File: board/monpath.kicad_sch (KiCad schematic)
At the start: 120 parts, among them J2 BEL_FUSE_0826-1G1T-23-F, J8 BEL_FUSE_0826-1G1T-23-F, U10 ECS-2016MVQ-250-CN-TR, U11 ECS-2016MVQ-250-CN-TR, U12 ECS-2016MVQ-250-CN-TR, U2 KSZ9031RN, U4 XC7S15-1FTGB196C, U9 KSZ9031RN

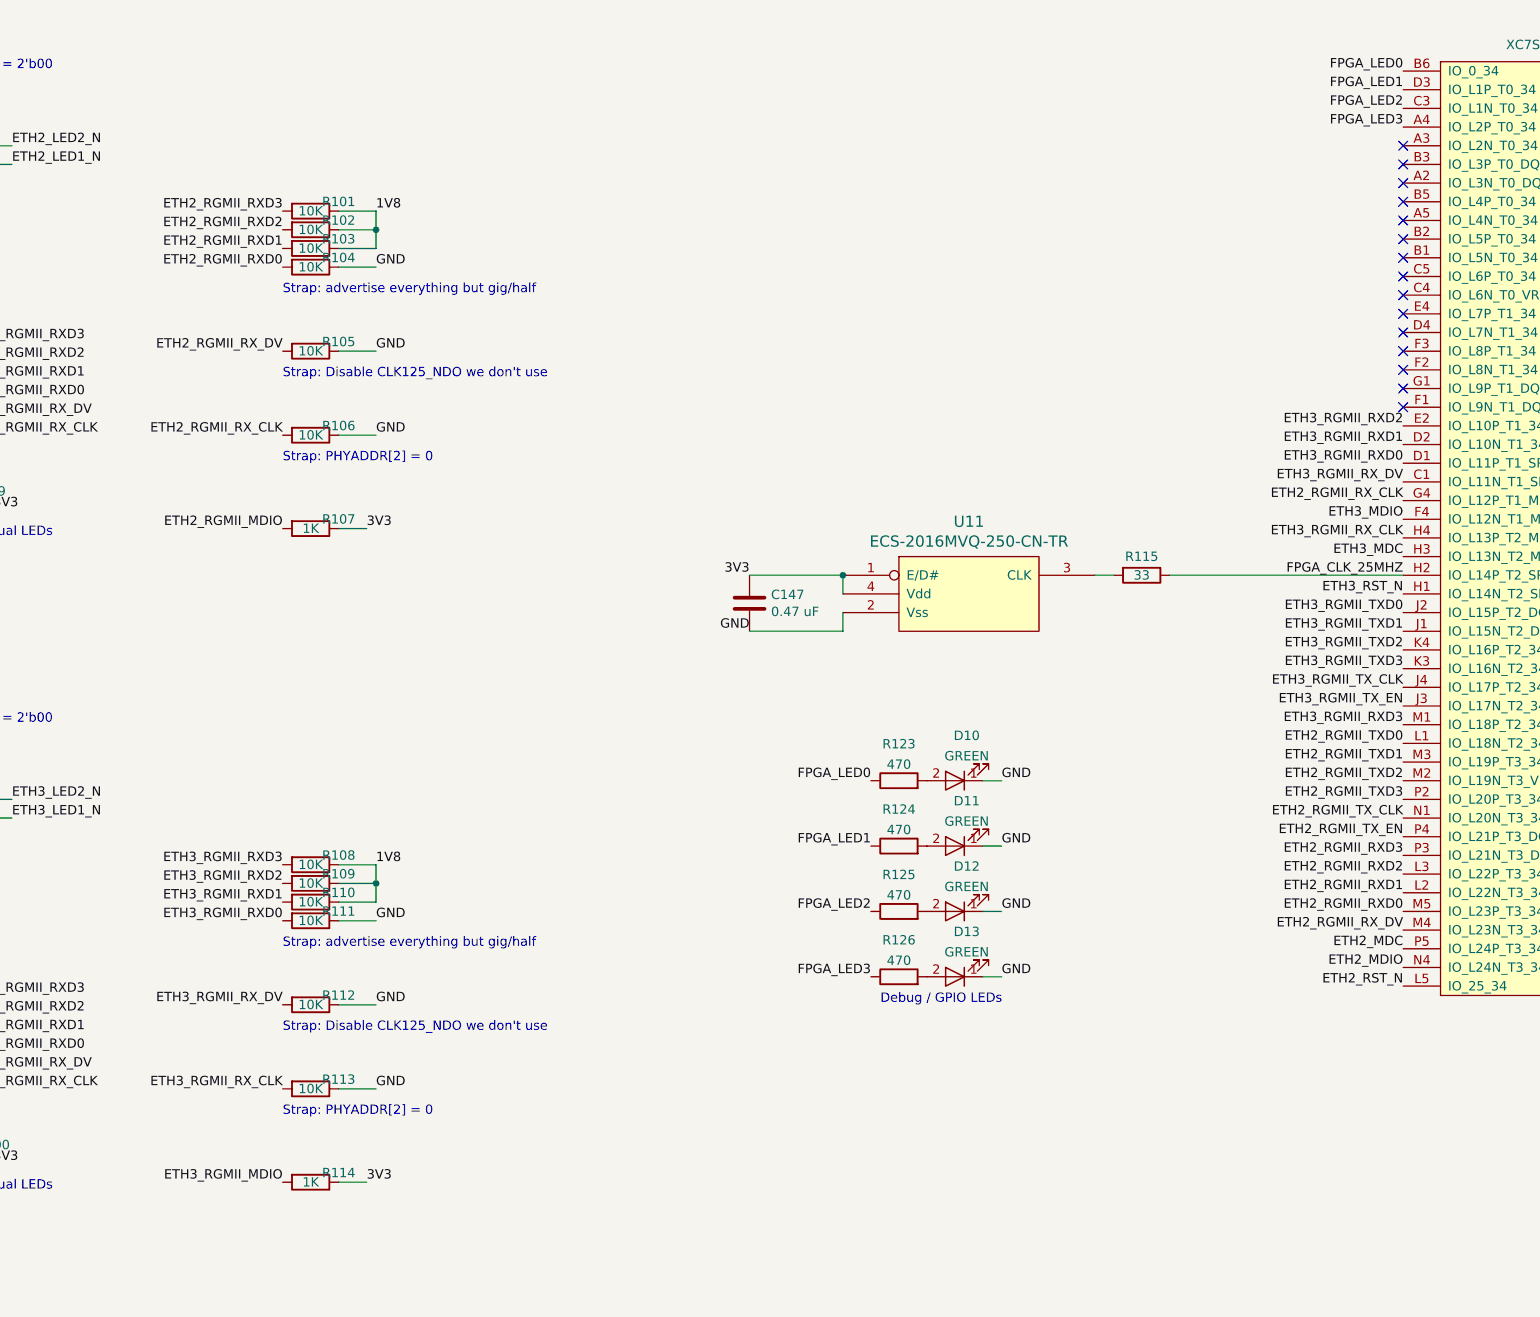
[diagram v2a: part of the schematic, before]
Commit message: Continued initial layout. First PHY fully routed including connection to FPGA. Hooked up 0402 bypass caps under FPGA. Flash is roughly placed.
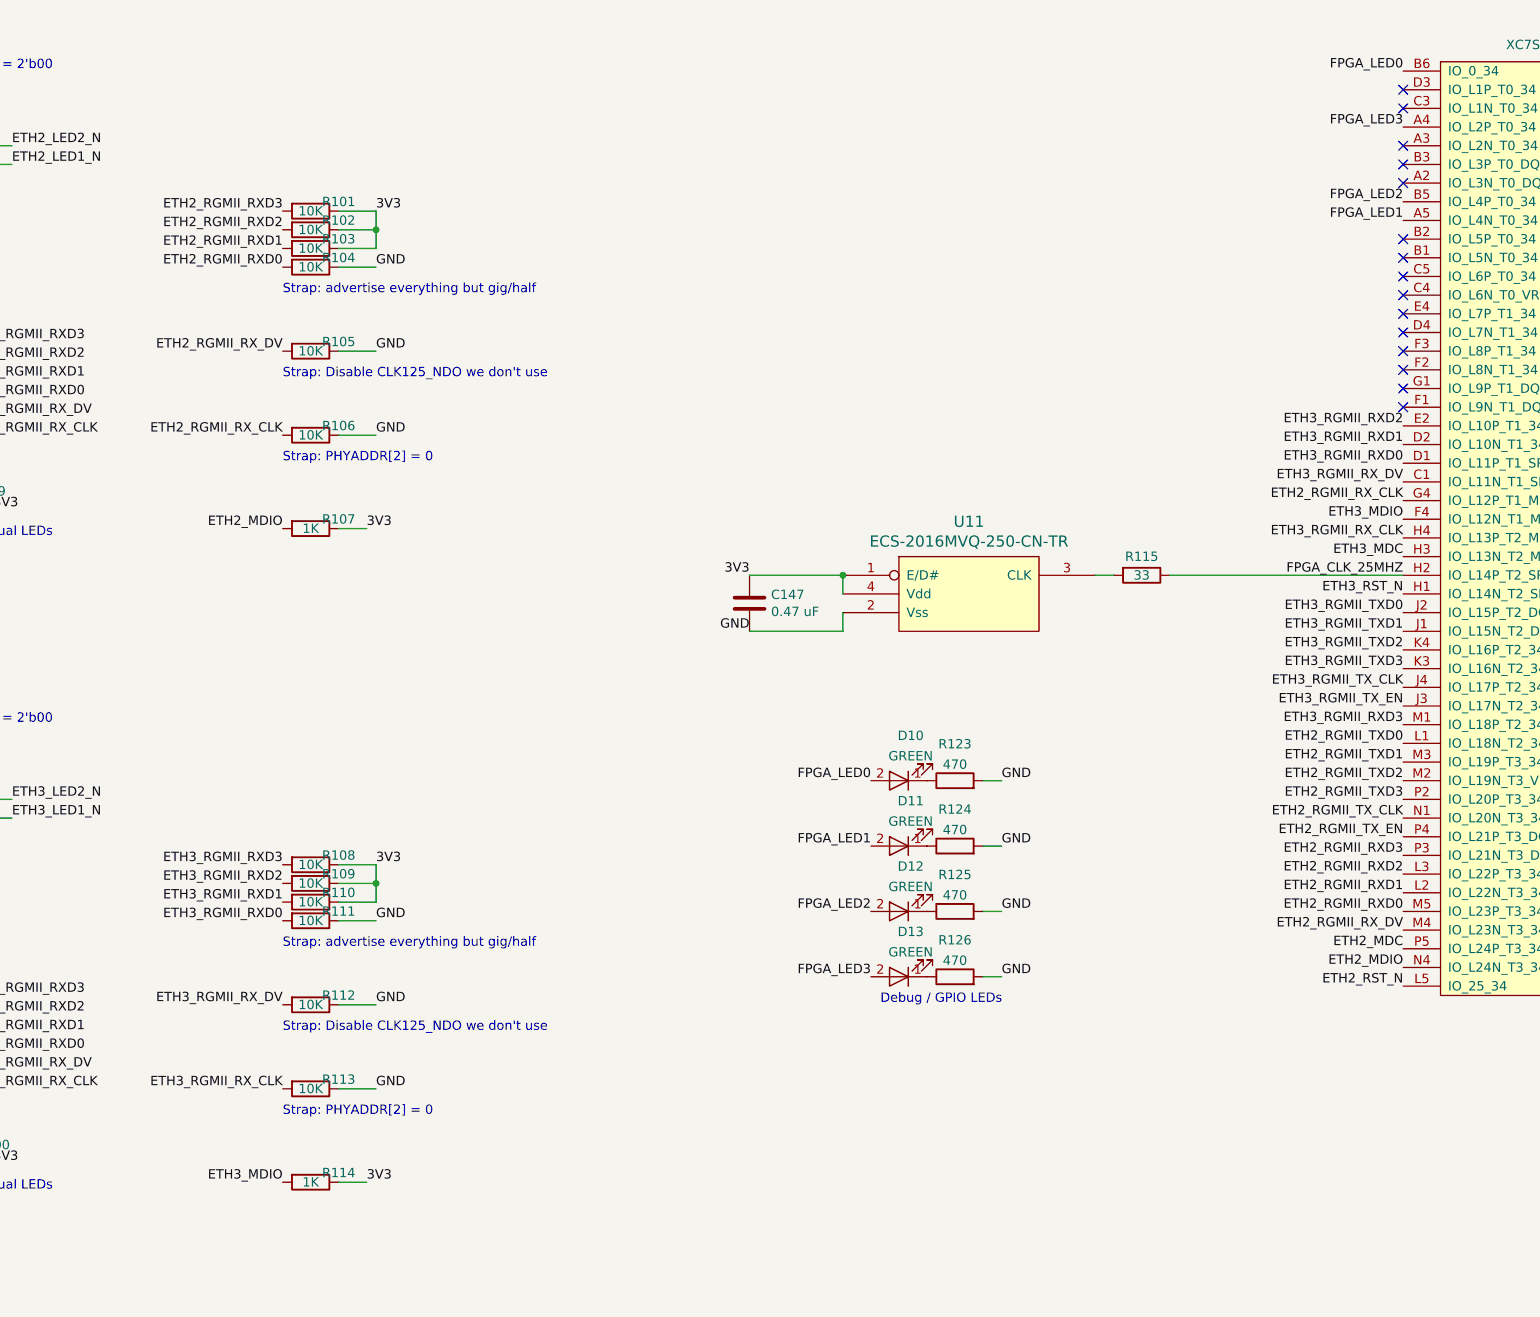
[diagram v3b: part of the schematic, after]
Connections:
- net 1V8 is gone; now on net 3V3: R101.1, R102.1, R103.1, R108.1, R109.1, R110.1
- net ETH2_RGMII_MDIO is gone; now on net ETH2_MDIO: R107.2
- net ETH3_RGMII_MDIO is gone; now on net ETH3_MDIO: R114.2
- net FPGA_LED0: now also D10.2 (A); no longer R123.1
- net FPGA_LED1: now also D11.2 (A), U4.A5 (IO_L4N_T0_34); no longer R124.1, U4.D3 (IO_L1P_T0_34)
- net FPGA_LED2: now also D12.2 (A), U4.B5 (IO_L4P_T0_34); no longer R125.1, U4.C3 (IO_L1N_T0_34)
- net FPGA_LED3: now also D13.2 (A); no longer R126.1
- net GND: now also R123.2, R124.2, R125.2, R126.2; no longer D10.1 (K), D11.1 (K), D12.1 (K), D13.1 (K)
- new net: D13.1 (K), R126.1
- new net: D12.1 (K), R125.1
- new net: D11.1 (K), R124.1
- new net: D10.1 (K), R123.1
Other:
- moved on the sheet: D10, D11, D12, D13, R123, R124, R125, R126
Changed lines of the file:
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@@
   (title_block
     (title "Active 10/100/1000baseT Tap")
-    (date "2022-12-20")
+    (date "2022-12-21")
     (rev "0.1")
     (company "Antikernel Labs")
@@
   (no_connect (at 365.76 35.56))
   (no_connect (at 95.25 72.39))
-  (no_connect (at 365.76 43.18))
   (no_connect (at 365.76 53.34))
   (no_connect (at 152.4 80.01))
@@
   (no_connect (at 365.76 63.5))
   (no_connect (at 95.25 161.29))
-  (no_connect (at 365.76 33.02))
+  (no_connect (at 365.76 25.4))
   (no_connect (at 152.4 180.34))
   (no_connect (at 152.4 91.44))
   (no_connect (at 365.76 60.96))
+  (no_connect (at 365.76 27.94))
   (no_connect (at 365.76 68.58))
-  (no_connect (at 365.76 40.64))
   (no_connect (at 365.76 38.1))
   (no_connect (at 365.76 58.42))
   (no_connect (at 152.4 168.91))
+  (no_connect (at 365.76 33.02))
   (wire (pts (xy 48.26 128.27) (xy 59.69 128.27))
     (stroke (width 0) (type default) (color 0 0 0 0))
@@
     (effects (font (size 1.27 1.27)) (justify right bottom))
   )
-  (label "FPGA_LED1" (at 365.76 25.4 180)
+  (label "FPGA_LED1" (at 365.76 43.18 180)
     (effects (font (size 1.27 1.27)) (justify right bottom))
   )
@@
     (effects (font (size 1.27 1.27)) (justify right bottom))
   )
-  (label "ETH2_RGMII_MDIO" (at 213.36 85.09 180)
+  (label "ETH2_MDIO" (at 213.36 85.09 180)
     (effects (font (size 1.27 1.27)) (justify right bottom))
   )
@@
     (effects (font (size 1.27 1.27)) (justify left bottom))
   )
-  (label "1V8" (at 226.06 41.91 0)
+  (label "3V3" (at 226.06 41.91 0)
     (effects (font (size 1.27 1.27)) (justify left bottom))
   )
@@
     (effects (font (size 1.27 1.27)) (justify right bottom))
   )
-  (label "FPGA_LED2" (at 365.76 27.94 180)
+  (label "FPGA_LED2" (at 365.76 40.64 180)
     (effects (font (size 1.27 1.27)) (justify right bottom))
   )
@@
     (effects (font (size 1.27 1.27)) (justify right bottom))
   )
-  (label "ETH3_RGMII_MDIO" (at 213.36 173.99 180)
+  (label "ETH3_MDIO" (at 213.36 173.99 180)
     (effects (font (size 1.27 1.27)) (justify right bottom))
   )
@@
     (effects (font (size 1.27 1.27)) (justify right bottom))
   )
-  (label "1V8" (at 226.06 130.81 0)
+  (label "3V3" (at 226.06 130.81 0)
     (effects (font (size 1.27 1.27)) (justify left bottom))
   )
@@
     (pin "2")
   )
-  (symbol (lib_id "device:LED") (at 304.8 146.05 180) (unit 1)
+  (symbol (lib_id "device:LED") (at 297.18 146.05 180) (unit 1)
     (in_bom yes) (on_board yes) (fields_autoplaced)
-    (property "Reference" "D13" (id 0) (at 306.4002 139.9245 0))
-    (property "Value" "GREEN" (id 1) (at 306.4002 142.6996 0))
-    (property "Footprint" "azonenberg_pcb:EIA_0603_LED" (id 2) (at 304.8 146.05 0)
+    (property "Reference" "D13" (id 0) (at 298.7802 139.9245 0))
+    (property "Value" "GREEN" (id 1) (at 298.7802 142.6996 0))
+    (property "Footprint" "azonenberg_pcb:EIA_0603_LED" (id 2) (at 297.18 146.05 0)
       (effects (font (size 1.27 1.27)) hide)
     )
-    (property "Datasheet" "" (id 3) (at 304.8 146.05 0)
+    (property "Datasheet" "" (id 3) (at 297.18 146.05 0)
       (effects (font (size 1.27 1.27)) hide)
     )
@@
     (pin "2")
   )
-  (symbol (lib_id "device:LED") (at 304.8 137.16 180) (unit 1)
+  (symbol (lib_id "device:LED") (at 297.18 137.16 180) (unit 1)
     (in_bom yes) (on_board yes) (fields_autoplaced)
-    (property "Reference" "D12" (id 0) (at 306.4002 131.0345 0))
-    (property "Value" "GREEN" (id 1) (at 306.4002 133.8096 0))
-    (property "Footprint" "azonenberg_pcb:EIA_0603_LED" (id 2) (at 304.8 137.16 0)
+    (property "Reference" "D12" (id 0) (at 298.7802 131.0345 0))
+    (property "Value" "GREEN" (id 1) (at 298.7802 133.8096 0))
+    (property "Footprint" "azonenberg_pcb:EIA_0603_LED" (id 2) (at 297.18 137.16 0)
       (effects (font (size 1.27 1.27)) hide)
     )
-    (property "Datasheet" "" (id 3) (at 304.8 137.16 0)
+    (property "Datasheet" "" (id 3) (at 297.18 137.16 0)
       (effects (font (size 1.27 1.27)) hide)
     )
@@
     (pin "2")
   )
-  (symbol (lib_id "device:LED") (at 304.8 128.27 180) (unit 1)
+  (symbol (lib_id "device:LED") (at 297.18 128.27 180) (unit 1)
     (in_bom yes) (on_board yes) (fields_autoplaced)
-    (property "Reference" "D11" (id 0) (at 306.4002 122.1445 0))
-    (property "Value" "GREEN" (id 1) (at 306.4002 124.9196 0))
-    (property "Footprint" "azonenberg_pcb:EIA_0603_LED" (id 2) (at 304.8 128.27 0)
+    (property "Reference" "D11" (id 0) (at 298.7802 122.1445 0))
+    (property "Value" "GREEN" (id 1) (at 298.7802 124.9196 0))
+    (property "Footprint" "azonenberg_pcb:EIA_0603_LED" (id 2) (at 297.18 128.27 0)
       (effects (font (size 1.27 1.27)) hide)
     )
-    (property "Datasheet" "" (id 3) (at 304.8 128.27 0)
+    (property "Datasheet" "" (id 3) (at 297.18 128.27 0)
       (effects (font (size 1.27 1.27)) hide)
     )
@@
     (pin "2")
   )
-  (symbol (lib_id "device:R") (at 297.18 137.16 90) (unit 1)
+  (symbol (lib_id "device:R") (at 304.8 137.16 90) (unit 1)
     (in_bom yes) (on_board yes) (fields_autoplaced)
-    (property "Reference" "R125" (id 0) (at 297.18 132.1775 90))
-    (property "Value" "470" (id 1) (at 297.18 134.9526 90))
-    (property "Footprint" "azonenberg_pcb:EIA_0402_RES_NOSILK" (id 2) (at 297.18 138.938 90)
+    (property "Reference" "R125" (id 0) (at 304.8 132.1775 90))
+    (property "Value" "470" (id 1) (at 304.8 134.9526 90))
+    (property "Footprint" "azonenberg_pcb:EIA_0402_RES_NOSILK" (id 2) (at 304.8 138.938 90)
       (effects (font (size 1.27 1.27)) hide)
     )
-    (property "Datasheet" "" (id 3) (at 297.18 137.16 0)
+    (property "Datasheet" "" (id 3) (at 304.8 137.16 0)
       (effects (font (size 1.27 1.27)) hide)
     )
@@
     (pin "2")
   )
-  (symbol (lib_id "device:R") (at 297.18 119.38 90) (unit 1)
+  (symbol (lib_id "device:R") (at 304.8 119.38 90) (unit 1)
     (in_bom yes) (on_board yes) (fields_autoplaced)
-    (property "Reference" "R123" (id 0) (at 297.18 114.3975 90))
-    (property "Value" "470" (id 1) (at 297.18 117.1726 90))
-    (property "Footprint" "azonenberg_pcb:EIA_0402_RES_NOSILK" (id 2) (at 297.18 121.158 90)
+    (property "Reference" "R123" (id 0) (at 304.8 114.3975 90))
+    (property "Value" "470" (id 1) (at 304.8 117.1726 90))
+    (property "Footprint" "azonenberg_pcb:EIA_0402_RES_NOSILK" (id 2) (at 304.8 121.158 90)
       (effects (font (size 1.27 1.27)) hide)
     )
-    (property "Datasheet" "" (id 3) (at 297.18 119.38 0)
+    (property "Datasheet" "" (id 3) (at 304.8 119.38 0)
       (effects (font (size 1.27 1.27)) hide)
     )
@@
     (pin "2")
   )
-  (symbol (lib_id "device:R") (at 297.18 128.27 90) (unit 1)
+  (symbol (lib_id "device:R") (at 304.8 128.27 90) (unit 1)
     (in_bom yes) (on_board yes) (fields_autoplaced)
-    (property "Reference" "R124" (id 0) (at 297.18 123.2875 90))
-    (property "Value" "470" (id 1) (at 297.18 126.0626 90))
-    (property "Footprint" "azonenberg_pcb:EIA_0402_RES_NOSILK" (id 2) (at 297.18 130.048 90)
+    (property "Reference" "R124" (id 0) (at 304.8 123.2875 90))
+    (property "Value" "470" (id 1) (at 304.8 126.0626 90))
+    (property "Footprint" "azonenberg_pcb:EIA_0402_RES_NOSILK" (id 2) (at 304.8 130.048 90)
       (effects (font (size 1.27 1.27)) hide)
     )
-    (property "Datasheet" "" (id 3) (at 297.18 128.27 0)
+    (property "Datasheet" "" (id 3) (at 304.8 128.27 0)
       (effects (font (size 1.27 1.27)) hide)
     )
@@
     (pin "2")
   )
-  (symbol (lib_id "device:LED") (at 304.8 119.38 180) (unit 1)
+  (symbol (lib_id "device:LED") (at 297.18 119.38 180) (unit 1)
     (in_bom yes) (on_board yes) (fields_autoplaced)
-    (property "Reference" "D10" (id 0) (at 306.4002 113.2545 0))
-    (property "Value" "GREEN" (id 1) (at 306.4002 116.0296 0))
-    (property "Footprint" "azonenberg_pcb:EIA_0603_LED" (id 2) (at 304.8 119.38 0)
+    (property "Reference" "D10" (id 0) (at 298.7802 113.2545 0))
+    (property "Value" "GREEN" (id 1) (at 298.7802 116.0296 0))
+    (property "Footprint" "azonenberg_pcb:EIA_0603_LED" (id 2) (at 297.18 119.38 0)
       (effects (font (size 1.27 1.27)) hide)
     )
-    (property "Datasheet" "" (id 3) (at 304.8 119.38 0)
+    (property "Datasheet" "" (id 3) (at 297.18 119.38 0)
       (effects (font (size 1.27 1.27)) hide)
     )
@@
     (pin "2")
   )
-  (symbol (lib_id "device:R") (at 297.18 146.05 90) (unit 1)
+  (symbol (lib_id "device:R") (at 304.8 146.05 90) (unit 1)
     (in_bom yes) (on_board yes) (fields_autoplaced)
-    (property "Reference" "R126" (id 0) (at 297.18 141.0675 90))
-    (property "Value" "470" (id 1) (at 297.18 143.8426 90))
-    (property "Footprint" "azonenberg_pcb:EIA_0402_RES_NOSILK" (id 2) (at 297.18 147.828 90)
+    (property "Reference" "R126" (id 0) (at 304.8 141.0675 90))
+    (property "Value" "470" (id 1) (at 304.8 143.8426 90))
+    (property "Footprint" "azonenberg_pcb:EIA_0402_RES_NOSILK" (id 2) (at 304.8 147.828 90)
       (effects (font (size 1.27 1.27)) hide)
     )
-    (property "Datasheet" "" (id 3) (at 297.18 146.05 0)
+    (property "Datasheet" "" (id 3) (at 304.8 146.05 0)
       (effects (font (size 1.27 1.27)) hide)
     )
